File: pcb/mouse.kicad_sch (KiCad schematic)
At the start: 15 parts, among them J1 Conn_02x03_Counter_Clockwise, SW1 SW_MEC_5E, U1 STM32F042K6Tx, U3 TLV70018_SOT23-5, U4 TLV70033_SOT23-5

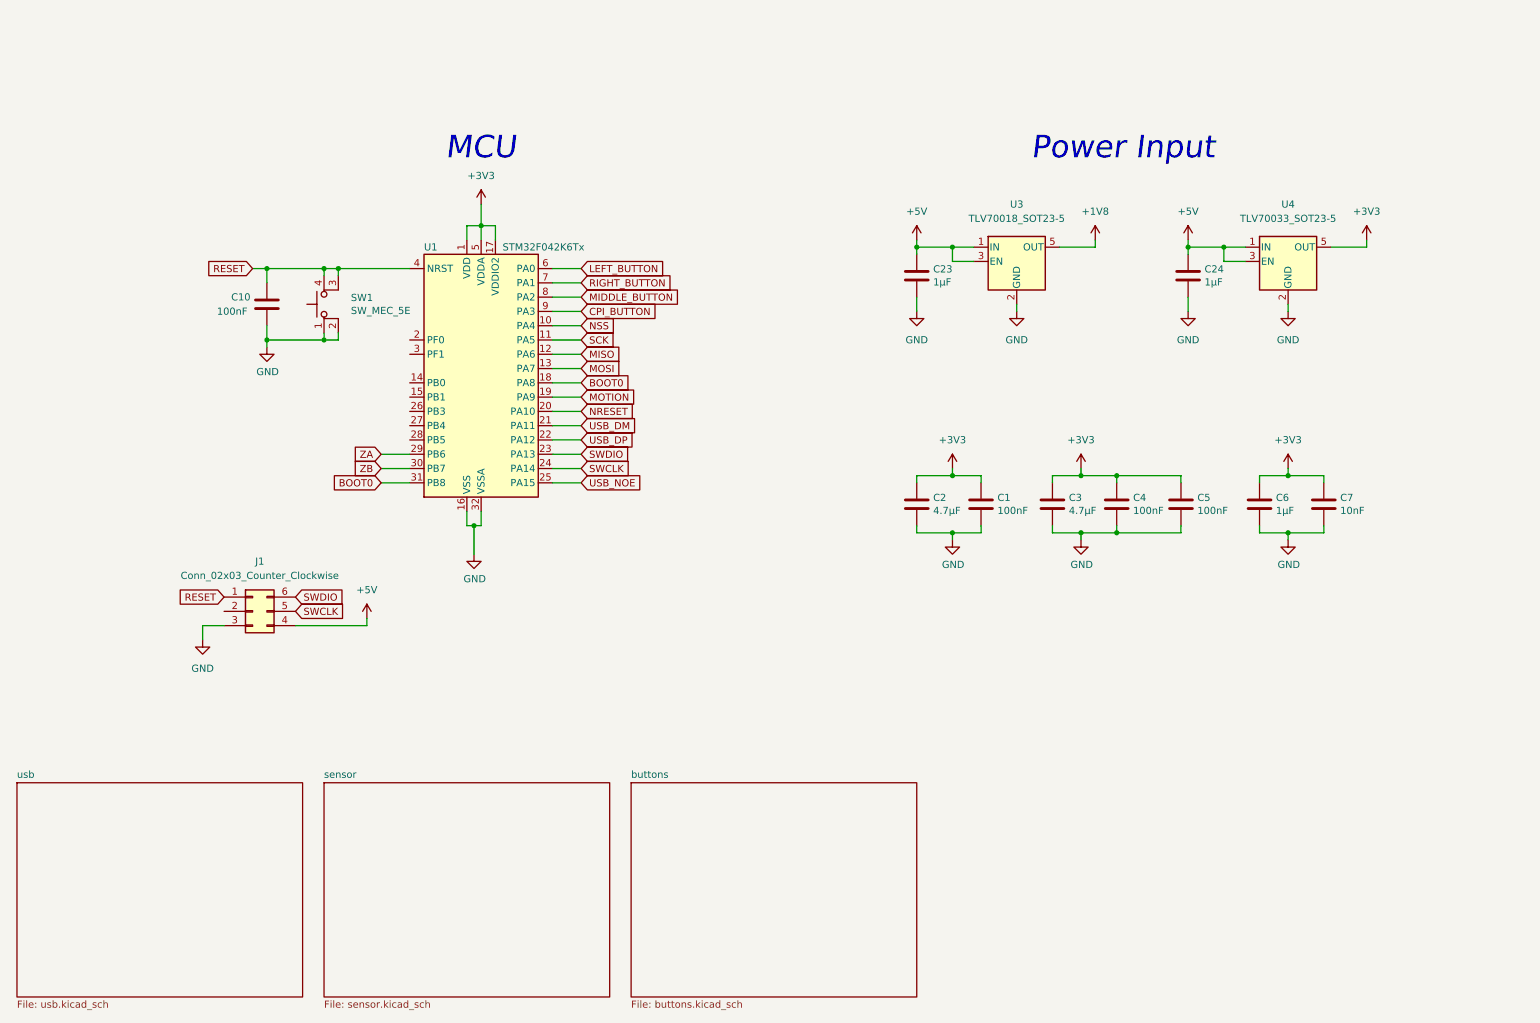
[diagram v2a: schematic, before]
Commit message: - split schematic to lists - changed global ports to local - assigned footprints to majority of schematic parts
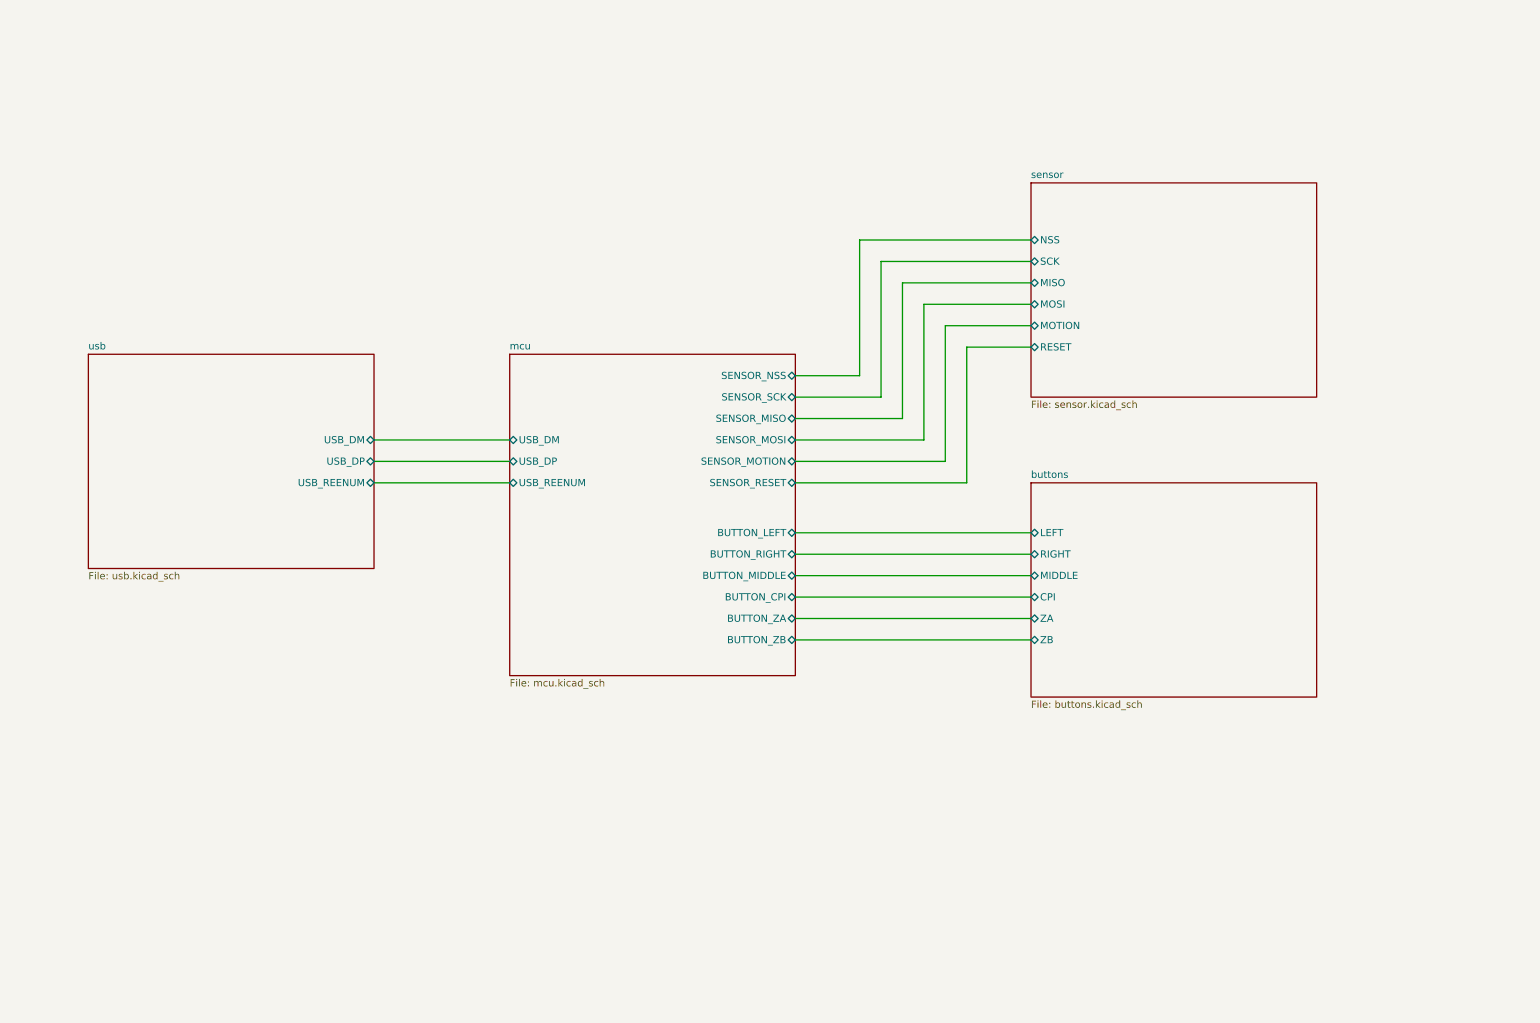
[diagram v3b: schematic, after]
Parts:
- removed C1, C10, C4, C5: 100nF, symbol Device:C
- removed C2, C3: 4.7μF, symbol Device:C
- removed C23, C24, C6: 1μF, symbol Device:C
- removed C7: 10nF, symbol Device:C
- removed J1: Conn_02x03_Counter_Clockwise, symbol Connector_Generic:Conn_02x03_Counter_Clockwise
- removed SW1: SW_MEC_5E, symbol Switch:SW_MEC_5E
- removed U1: STM32F042K6Tx, Package_QFP:LQFP-32_7x7mm_P0.8mm, symbol MCU_ST_STM32F0:STM32F042K6Tx
- removed U3: TLV70018_SOT23-5, Package_TO_SOT_SMD:SOT-23-5, symbol Regulator_Linear:TLV70018_SOT23-5
- removed U4: TLV70033_SOT23-5, Package_TO_SOT_SMD:SOT-23-5, symbol Regulator_Linear:TLV70033_SOT23-5
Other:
- added sheet mcu (mcu.kicad_sch)
- sheet buttons ports: added CPI, LEFT, MIDDLE, RIGHT, ZA, ZB; removed none
- sheet sensor ports: added MISO, MOSI, MOTION, NSS, RESET, SCK; removed none
- sheet usb ports: added USB_DM, USB_DP, USB_REENUM; removed none
- note removed: "MCU"
- note removed: "Power Input"

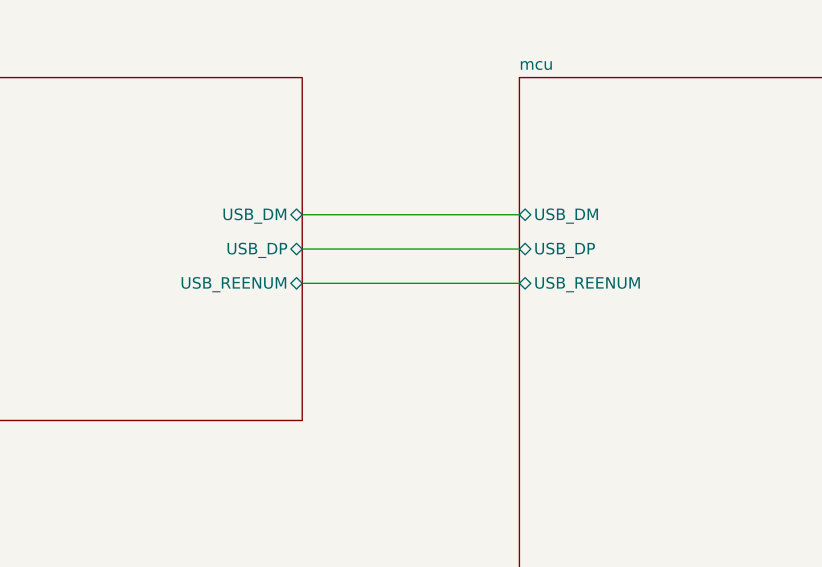
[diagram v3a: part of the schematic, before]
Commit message: - added debouncing to buttons - assigned some footprints - added expansion and inspection pin headers
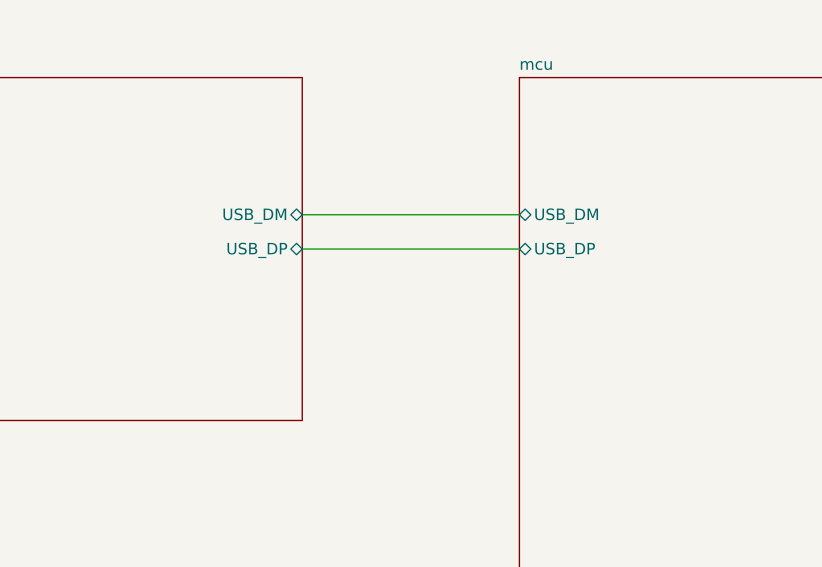
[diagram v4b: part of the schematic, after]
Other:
- sheet mcu ports: added none; removed USB_REENUM
- sheet usb ports: added none; removed USB_REENUM
